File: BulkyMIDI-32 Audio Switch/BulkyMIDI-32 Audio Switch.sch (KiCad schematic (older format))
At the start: 44 parts, among them J1 DC IN, J10 OUT, J4 Conn_Power, J6 Switch Panel, M1 Mounting, M2 Mounting, M3 Mounting, M4 Mounting, SW1 CH1, SW2 CH2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

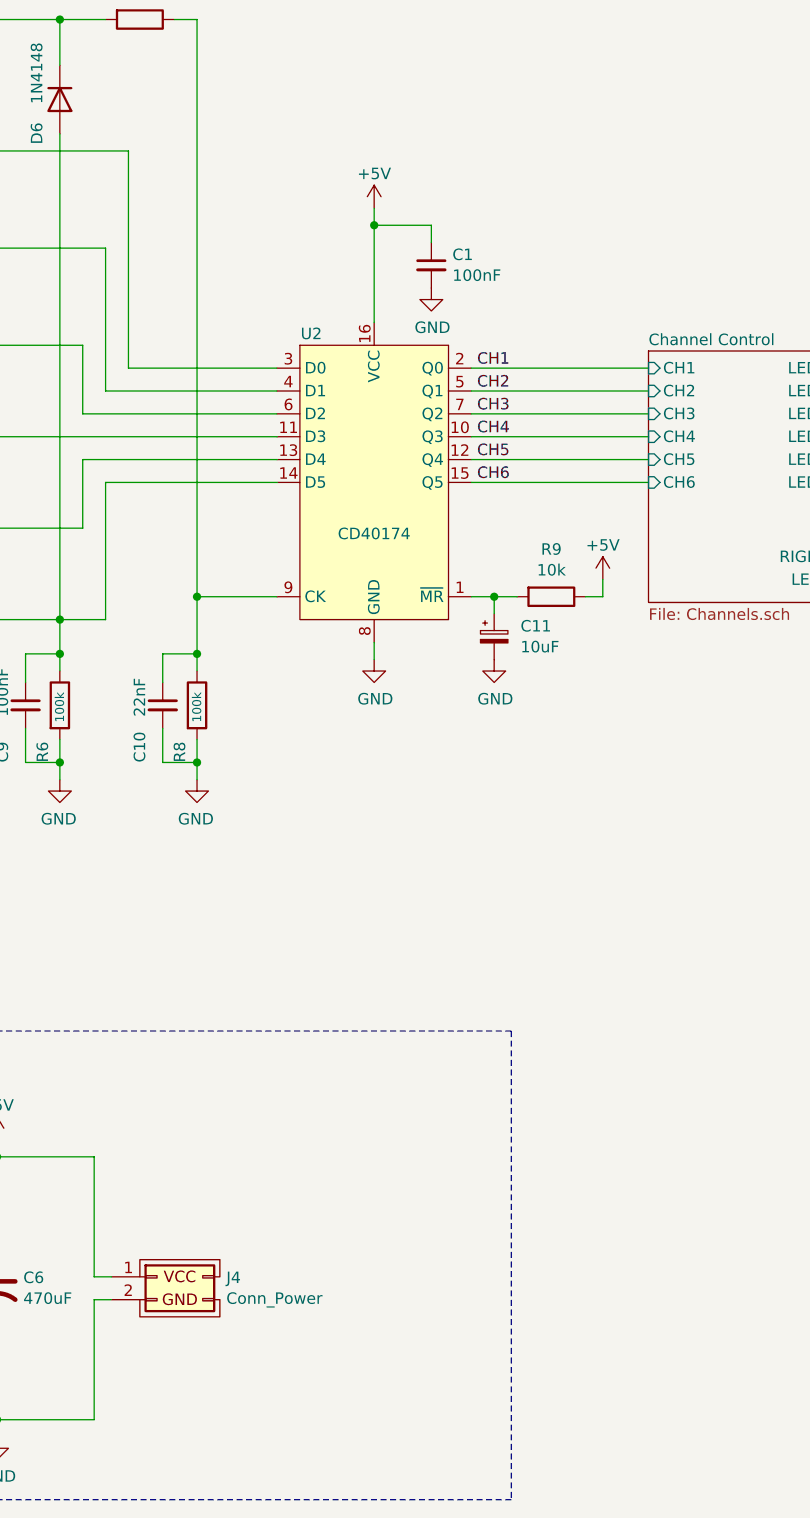
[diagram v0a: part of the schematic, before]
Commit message: Untested audio switch module
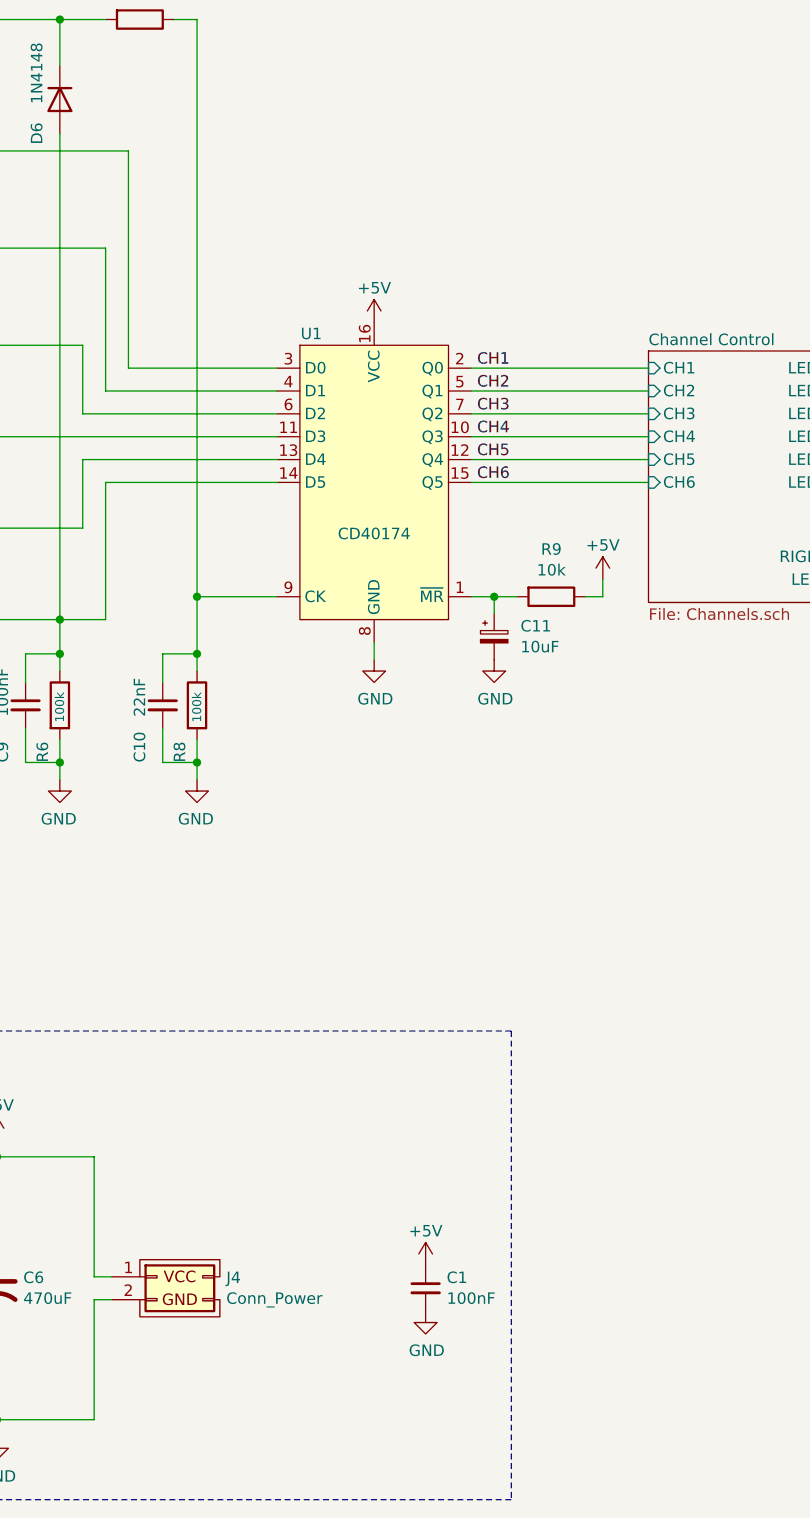
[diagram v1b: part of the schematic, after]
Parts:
- R1, R2, R28, R3, R4, R5, R6, R7, R8, R9: footprint Resistor_THT:R_Axial_DIN0207_L6.3mm_D2.5mm_P10.16mm_Horizontal -> resistor:R_Axial_DIN0207_L6.3mm_D2.5mm_P10.16mm_Horizontal
- renumbered U2 to U1
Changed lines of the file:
@@
 Connection ~ 950  3200
 $Comp
-L cd40174:CD40174 U2
+L cd40174:CD40174 U1
 U 1 1 62D697D7
 P 5050 2900
-F 0 "U2" H 4775 3450 50  0000 C CNN
+F 0 "U1" H 4775 3450 50  0000 C CNN
 F 1 "CD40174" H 5050 2575 50  0000 C CNN
 F 2 "Package_DIP:DIP-16_W10.16mm_LongPads" H 5050 2900 50  0001 C CNN
@@
 L power:+5V #PWR0102
 U 1 1 62D6B55A
-P 5050 1800
-F 0 "#PWR0102" H 5050 1650 50  0001 C CNN
-F 1 "+5V" H 5050 1950 50  0000 C CNN
-F 2 "" H 5050 1800 50  0001 C CNN
-F 3 "" H 5050 1800 50  0001 C CNN
-	1    5050 1800
+P 5050 2300
+F 0 "#PWR0102" H 5050 2150 50  0001 C CNN
+F 1 "+5V" H 5050 2450 50  0000 C CNN
+F 2 "" H 5050 2300 50  0001 C CNN
+F 3 "" H 5050 2300 50  0001 C CNN
+	1    5050 2300
 	1    0    0    -1
 $EndComp
@@
 F 0 "R1" V 1850 3725 50  0000 L CNN
 F 1 "100k" V 1925 3900 39  0000 L CNN
-F 2 "Resistor_THT:R_Axial_DIN0207_L6.3mm_D2.5mm_P10.16mm_Horizontal" V 1855 3975 50  0001 C CNN
+F 2 "resistor:R_Axial_DIN0207_L6.3mm_D2.5mm_P10.16mm_Horizontal" V 1855 3975 50  0001 C CNN
 F 3 "~" H 1925 3975 50  0001 C CNN
 	1    1925 3975
@@
 F 0 "R2" V 2200 3725 50  0000 L CNN
 F 1 "100k" V 2275 3900 39  0000 L CNN
-F 2 "Resistor_THT:R_Axial_DIN0207_L6.3mm_D2.5mm_P10.16mm_Horizontal" V 2205 3975 50  0001 C CNN
+F 2 "resistor:R_Axial_DIN0207_L6.3mm_D2.5mm_P10.16mm_Horizontal" V 2205 3975 50  0001 C CNN
 F 3 "~" H 2275 3975 50  0001 C CNN
 	1    2275 3975
@@
 F 0 "R3" V 2550 3725 50  0000 L CNN
 F 1 "100k" V 2625 3900 39  0000 L CNN
-F 2 "Resistor_THT:R_Axial_DIN0207_L6.3mm_D2.5mm_P10.16mm_Horizontal" V 2555 3975 50  0001 C CNN
+F 2 "resistor:R_Axial_DIN0207_L6.3mm_D2.5mm_P10.16mm_Horizontal" V 2555 3975 50  0001 C CNN
 F 3 "~" H 2625 3975 50  0001 C CNN
 	1    2625 3975
@@
 F 0 "R4" V 2900 3725 50  0000 L CNN
 F 1 "100k" V 2975 3900 39  0000 L CNN
-F 2 "Resistor_THT:R_Axial_DIN0207_L6.3mm_D2.5mm_P10.16mm_Horizontal" V 2905 3975 50  0001 C CNN
+F 2 "resistor:R_Axial_DIN0207_L6.3mm_D2.5mm_P10.16mm_Horizontal" V 2905 3975 50  0001 C CNN
 F 3 "~" H 2975 3975 50  0001 C CNN
 	1    2975 3975
@@
 F 0 "R5" V 3250 3725 50  0000 L CNN
 F 1 "100k" V 3325 3900 39  0000 L CNN
-F 2 "Resistor_THT:R_Axial_DIN0207_L6.3mm_D2.5mm_P10.16mm_Horizontal" V 3255 3975 50  0001 C CNN
+F 2 "resistor:R_Axial_DIN0207_L6.3mm_D2.5mm_P10.16mm_Horizontal" V 3255 3975 50  0001 C CNN
 F 3 "~" H 3325 3975 50  0001 C CNN
 	1    3325 3975
@@
 F 0 "R6" V 3600 3725 50  0000 L CNN
 F 1 "100k" V 3675 3900 39  0000 L CNN
-F 2 "Resistor_THT:R_Axial_DIN0207_L6.3mm_D2.5mm_P10.16mm_Horizontal" V 3605 3975 50  0001 C CNN
+F 2 "resistor:R_Axial_DIN0207_L6.3mm_D2.5mm_P10.16mm_Horizontal" V 3605 3975 50  0001 C CNN
 F 3 "~" H 3675 3975 50  0001 C CNN
 	1    3675 3975
@@
 F 0 "R8" V 4200 3725 50  0000 L CNN
 F 1 "100k" V 4275 3900 39  0000 L CNN
-F 2 "Resistor_THT:R_Axial_DIN0207_L6.3mm_D2.5mm_P10.16mm_Horizontal" V 4205 3975 50  0001 C CNN
+F 2 "resistor:R_Axial_DIN0207_L6.3mm_D2.5mm_P10.16mm_Horizontal" V 4205 3975 50  0001 C CNN
 F 3 "~" H 4275 3975 50  0001 C CNN
 	1    4275 3975
@@
 F 0 "R7" V 3818 975 50  0000 C CNN
 F 1 "10k" V 3909 975 50  0000 C CNN
-F 2 "Resistor_THT:R_Axial_DIN0207_L6.3mm_D2.5mm_P10.16mm_Horizontal" V 3955 975 50  0001 C CNN
+F 2 "resistor:R_Axial_DIN0207_L6.3mm_D2.5mm_P10.16mm_Horizontal" V 3955 975 50  0001 C CNN
 F 3 "~" H 4025 975 50  0001 C CNN
 	1    4025 975
@@
 F 0 "R9" V 5618 3500 50  0000 C CNN
 F 1 "10k" V 5709 3500 50  0000 C CNN
-F 2 "Resistor_THT:R_Axial_DIN0207_L6.3mm_D2.5mm_P10.16mm_Horizontal" V 5755 3500 50  0001 C CNN
+F 2 "resistor:R_Axial_DIN0207_L6.3mm_D2.5mm_P10.16mm_Horizontal" V 5755 3500 50  0001 C CNN
 F 3 "~" H 5825 3500 50  0001 C CNN
 	1    5825 3500
@@
 Wire Wire Line
 	950  3600 950  4025
-$Comp
-L Device:C_Small C1
-U 1 1 632D8AEB
-P 5300 2050
-F 0 "C1" H 5392 2096 50  0000 L CNN
-F 1 "100nF" H 5392 2005 50  0000 L CNN
-F 2 "Capacitor_THT:C_Disc_D4.7mm_W2.5mm_P5.00mm" H 5300 2050 50  0001 C CNN
-F 3 "~" H 5300 2050 50  0001 C CNN
-	1    5300 2050
-	1    0    0    -1
-$EndComp
-$Comp
-L power:GND #PWR0103
-U 1 1 632DB821
-P 5300 2150
-F 0 "#PWR0103" H 5300 1900 50  0001 C CNN
-F 1 "GND" H 5305 1977 50  0000 C CNN
-F 2 "" H 5300 2150 50  0001 C CNN
-F 3 "" H 5300 2150 50  0001 C CNN
-	1    5300 2150
-	1    0    0    -1
-$EndComp
-Wire Wire Line
-	5300 1950 5300 1875
-Wire Wire Line
-	5300 1875 5050 1875
-Wire Wire Line
-	5050 1875 5050 2300
-Wire Wire Line
-	5050 1800 5050 1875
-Connection ~ 5050 1875
 Text Label 5500 2500 0    50   ~ 0
 CH1
@@
 F 0 "R28" H 8880 2754 50  0000 R CNN
 F 1 "470" H 8880 2845 50  0000 R CNN
-F 2 "Resistor_THT:R_Axial_DIN0207_L6.3mm_D2.5mm_P10.16mm_Horizontal" V 8880 2800 50  0001 C CNN
+F 2 "resistor:R_Axial_DIN0207_L6.3mm_D2.5mm_P10.16mm_Horizontal" V 8880 2800 50  0001 C CNN
 F 3 "~" H 8950 2800 50  0001 C CNN
 	1    8950 2800
@@
 Wire Wire Line
 	8275 2575 8950 2575
+Connection ~ 8950 2575
+Wire Wire Line
+	8950 2575 8950 2650
+$Comp
+L Device:C_Small C1
+U 1 1 641084E6
+P 5275 6525
+F 0 "C1" H 5367 6571 50  0000 L CNN
+F 1 "100nF" H 5367 6480 50  0000 L CNN
+F 2 "Capacitor_THT:C_Disc_D4.7mm_W2.5mm_P5.00mm" H 5275 6525 50  0001 C CNN
+F 3 "~" H 5275 6525 50  0001 C CNN
+	1    5275 6525
+	1    0    0    -1
+$EndComp
+$Comp
+L power:GND #PWR0103
+U 1 1 641084EC
+P 5275 6625
+F 0 "#PWR0103" H 5275 6375 50  0001 C CNN
+F 1 "GND" H 5280 6452 50  0000 C CNN
+F 2 "" H 5275 6625 50  0001 C CNN
+F 3 "" H 5275 6625 50  0001 C CNN
+	1    5275 6625
+	1    0    0    -1
+$EndComp
+$Comp
+L power:+5V #PWR0145
+U 1 1 6410FE82
+P 5275 6425
+F 0 "#PWR0145" H 5275 6275 50  0001 C CNN
+F 1 "+5V" H 5275 6575 50  0000 C CNN
+F 2 "" H 5275 6425 50  0001 C CNN
+F 3 "" H 5275 6425 50  0001 C CNN
+	1    5275 6425
+	1    0    0    -1
+$EndComp
 Wire Bus Line
 	7975 2400 7975 2900
 Wire Bus Line
 	9950 2400 9950 3675
-Connection ~ 8950 2575
-Wire Wire Line
-	8950 2575 8950 2650
 $EndSCHEMATC

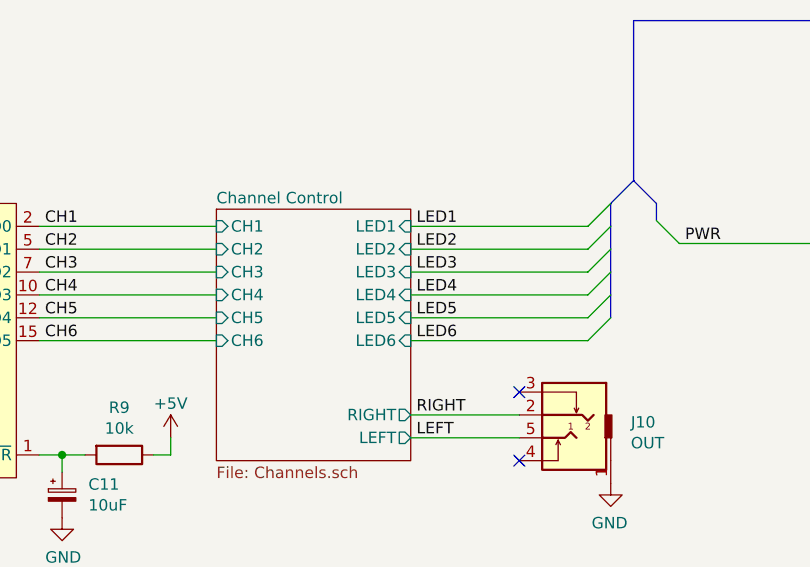
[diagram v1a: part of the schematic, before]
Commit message: Fix weird socket selection
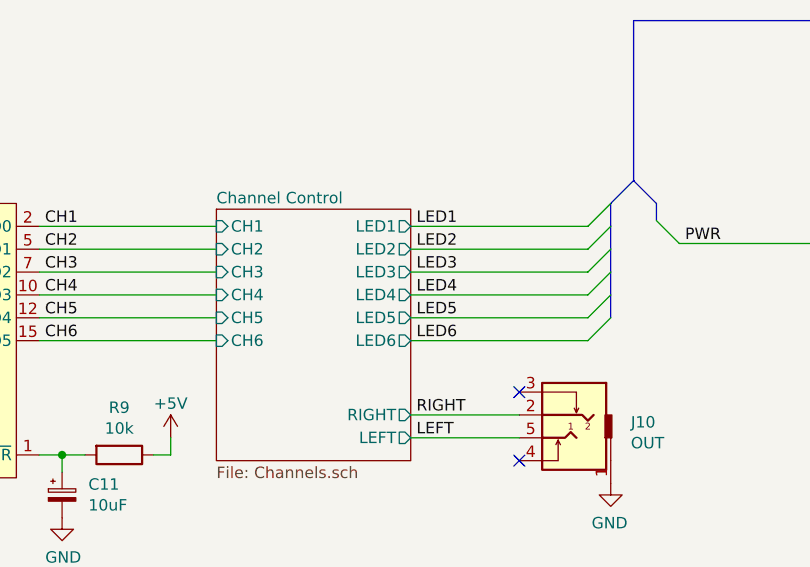
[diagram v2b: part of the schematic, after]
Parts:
- U1: footprint Package_DIP:DIP-16_W10.16mm_LongPads -> Package_DIP:DIP-16_W7.62mm_Socket_LongPads
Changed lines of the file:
@@
 F 0 "U1" H 4775 3450 50  0000 C CNN
 F 1 "CD40174" H 5050 2575 50  0000 C CNN
-F 2 "Package_DIP:DIP-16_W10.16mm_LongPads" H 5050 2900 50  0001 C CNN
+F 2 "Package_DIP:DIP-16_W7.62mm_Socket_LongPads" H 5050 2900 50  0001 C CNN
 F 3 "http://www.ti.com/lit/ds/symlink/sn74hc595.pdf" H 5050 2900 50  0001 C CNN
 	1    5050 2900
@@
 F6 "CH5" I L 6250 2900 50
 F7 "CH6" I L 6250 3000 50
-F8 "LED1" I R 7100 2500 50
-F9 "LED2" I R 7100 2600 50
-F10 "LED3" I R 7100 2700 50
-F11 "LED4" I R 7100 2800 50
-F12 "LED5" I R 7100 2900 50
-F13 "LED6" I R 7100 3000 50
+F8 "LED1" O R 7100 2500 50
+F9 "LED2" O R 7100 2600 50
+F10 "LED3" O R 7100 2700 50
+F11 "LED4" O R 7100 2800 50
+F12 "LED5" O R 7100 2900 50
+F13 "LED6" O R 7100 3000 50
 F14 "RIGHT" O R 7100 3325 50
 F15 "LEFT" O R 7100 3425 50

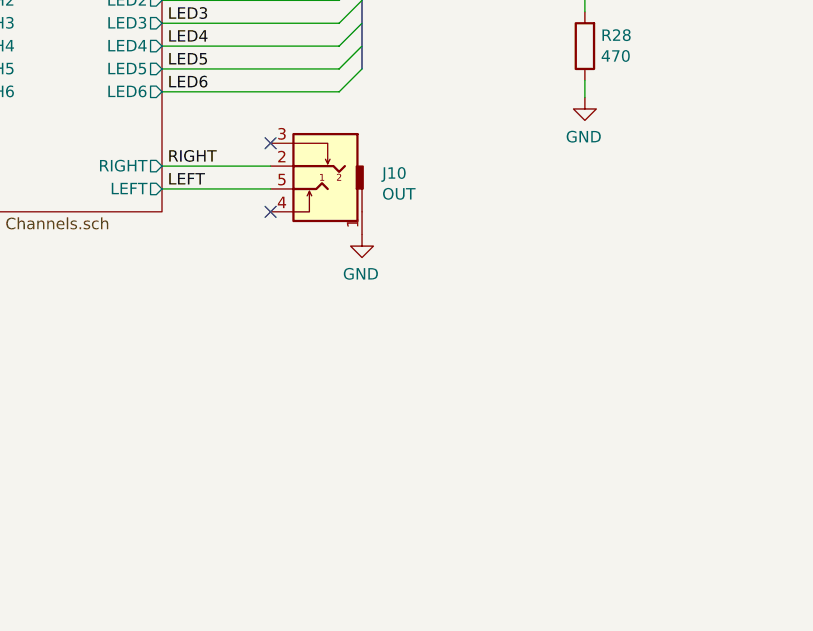
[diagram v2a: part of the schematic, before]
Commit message: Added alternate output placement
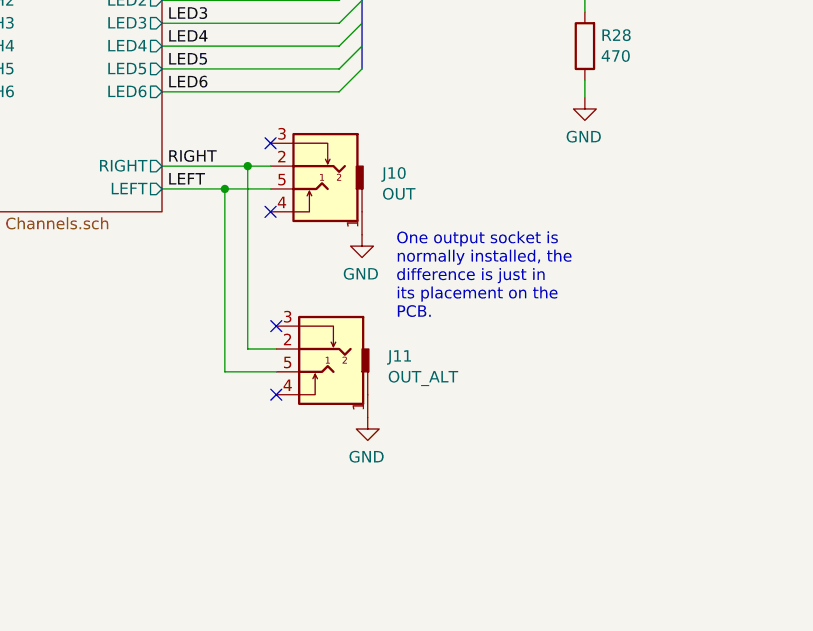
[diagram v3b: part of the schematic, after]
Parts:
- added J11: OUT_ALT, audio_jack:Tayda_3.5mm_stereo_TRS_jack_A-853, symbol audio_jack:TRS_3.5mm
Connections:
- net GND: now also J11.1
- net LEFT: now also J11.5
- net RIGHT: now also J11.2
- no-connect marks 3 -> 5
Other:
- note added: "One output socket is\nnormally installed, the\ndifference is just in \nits placement on the\nPCB."
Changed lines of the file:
@@
 Title "BulkyMIDI-32 Audio Switch"
 Date ""
-Rev "A"
+Rev "B"
 Comp ""
 Comment1 ""
@@
 $EndComp
 Wire Wire Line
-	7100 3325 7575 3325
-Wire Wire Line
-	7100 3425 7575 3425
+	7100 3325 7475 3325
+Wire Wire Line
+	7100 3425 7375 3425
 Text Label 7125 3325 0    50   ~ 0
 RIGHT
@@
 	1    0    0    -1
 $EndComp
+NoConn ~ 7600 4025
+NoConn ~ 7600 4325
+$Comp
+L audio_jack:TRS_3.5mm J11
+U 1 1 633D58B5
+P 7800 4225
+AR Path="/633D58B5" Ref="J11"  Part="1"
+AR Path="/635D4EBA/633D58B5" Ref="J?"  Part="1"
+F 0 "J11" H 7512 4293 50  0000 R CNN
+F 1 "OUT_ALT" H 7512 4202 50  0000 R CNN
+F 2 "audio_jack:Tayda_3.5mm_stereo_TRS_jack_A-853" H 8050 4325 50  0001 C CNN
+F 3 "~" H 8050 4325 50  0001 C CNN
+	1    7800 4225
+	-1   0    0    -1
+$EndComp
+$Comp
+L power:GND #PWR0119
+U 1 1 633D58BB
+P 8000 4425
+AR Path="/633D58BB" Ref="#PWR0119"  Part="1"
+AR Path="/635D4EBA/633D58BB" Ref="#PWR?"  Part="1"
+F 0 "#PWR0119" H 8000 4175 50  0001 C CNN
+F 1 "GND" H 8005 4252 50  0000 C CNN
+F 2 "" H 8000 4425 50  0001 C CNN
+F 3 "" H 8000 4425 50  0001 C CNN
+	1    8000 4425
+	-1   0    0    -1
+$EndComp
+Wire Wire Line
+	7375 3425 7375 4225
+Wire Wire Line
+	7375 4225 7600 4225
+Connection ~ 7375 3425
+Wire Wire Line
+	7375 3425 7575 3425
+Wire Wire Line
+	7475 3325 7475 4125
+Wire Wire Line
+	7475 4125 7600 4125
 Wire Bus Line
 	7975 2400 7975 2900
 Wire Bus Line
 	9950 2400 9950 3675
+Connection ~ 7475 3325
+Wire Wire Line
+	7475 3325 7575 3325
+Text Notes 8125 4000 0    50   ~ 0
+One output socket is\nnormally installed, the\ndifference is just in \nits placement on the\nPCB.
 $EndSCHEMATC
